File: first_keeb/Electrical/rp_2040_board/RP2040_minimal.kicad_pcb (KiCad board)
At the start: 2 copper layers, 77.4 x 77.1 mm, 72 parts, among them P1 USB-TYPE-C-016, Q1 SN74LV1T34DBV, SW1 SKRKAHE020, SW2 PTS647 SN70 SMTR2 LFS, SW3 PTS647 SN70 SMTR2 LFS, U1 NCP1117-3.3_SOT223, U2 LM4040DBZ-3, U3 PRTR5V0U2X, U4 W25Q32JVSS, U5 RP2040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

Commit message: stm it up
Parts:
- removed H4, H5: MountingHole_4.3mm_M4, MountingHole:MountingHole_4.3mm_M4
- SW2, SW3: footprint Button_Switch_SMD:PTS647_4.5x4.5mm -> Button_Switch_SMD:SW_Push_1P1T_NO_6x6mm_H9.5mm
- moved C13 48.7 mm to (146.7, 85.0)
- moved U2 48.7 mm to (157.4, 85.3)
- moved C14 48.7 mm to (148.5, 85.5)
- moved R1 48.7 mm to (161.1, 86.2)
- moved R4 48.7 mm to (153.9, 86.3)
- moved C15 42.1 mm to (57.8, 49.6), turned to 180 degrees
- moved C12 41.5 mm to (64.3, 67.8)
- moved C10 41.1 mm to (51.7, 64.2)
- moved C11 41.1 mm to (64.8, 66.8)
- moved C16 41.1 mm to (49.5, 60.3)
- moved C17 41.1 mm to (49.5, 63.3)
- moved C3 41.1 mm to (64.6, 62.7)
- moved C4 41.1 mm to (52.3, 65.7)
- moved C5 41.1 mm to (64.6, 63.8)
- moved C6 41.1 mm to (56.5, 59.1)
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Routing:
- net +5V: track 335.9 -> 22.7 mm, vias 14 -> 2
- net +3V3: track 275.9 -> 28.4 mm, vias 2 -> 0
- net Net-(D2-DOUT): track 30.3 -> 1.98 mm
- net Net-(D3-DOUT): track 30.4 -> 2.38 mm
- net Net-(D5-DOUT): track 30.8 -> 2.83 mm
- net Net-(D1-DOUT): track 27.6 -> 2.40 mm
- net Net-(D10-DOUT): track 25.9 -> 3.06 mm
- net /USB_D-: track 23.6 -> 7.99 mm
- net /USB_D+: track 24.1 -> 9.21 mm
- net VBUS: track 20.1 -> 8.45 mm
- net LED_D_3V: track 11.6 -> 0.86 mm
- net RP_ADC1: track 16.1 -> 7.76 mm
- net RP_ADC0: track 21.2 -> 16.2 mm
- net RP_ADC2: track 31.0 -> 26.4 mm
- net GPIO18: track 64.1 -> 62.2 mm
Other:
- board size 77.4 x 77.1 mm -> 65 x 64.7 mm

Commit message: stm32 pcb almost done
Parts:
- moved C10 42.6 mm to (86.5, 88.9)
- moved C16 42.6 mm to (84.3, 85.0)
- moved C17 42.6 mm to (84.3, 87.9)
- moved R7 42.6 mm to (85.8, 74.2)
- moved C11 42.6 mm to (99.5, 91.5)
- moved C12 42.6 mm to (99.1, 92.5)
- moved C15 42.6 mm to (92.6, 74.3)
- moved C3 42.6 mm to (99.4, 87.4)
- moved C5 42.6 mm to (99.4, 88.5)
- moved C6 42.6 mm to (91.3, 83.8)
- moved C7 42.6 mm to (94.6, 83.8)
- moved C8 42.6 mm to (91.5, 93.5)
- moved C9 42.6 mm to (96.3, 93.6)
- moved R5 42.6 mm to (99.4, 89.5)
- moved R6 42.6 mm to (99.4, 90.5)
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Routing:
- net GPIO19: track 83.6 -> 24.1 mm
- net GPIO18: track 62.2 -> 9.68 mm
- net RP_ADC2: track 26.4 -> 0.00 mm
- net Net-(D6-DOUT): track 29.2 -> 3.32 mm
- net RP_ADC0: track 16.2 -> 0.00 mm
- net RP_ADC1: track 7.76 -> 0.00 mm
- net +5V: track 22.7 -> 25.7 mm, vias 2 -> 4
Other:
- board size 65 x 64.7 mm -> 67.1 x 66.8 mm

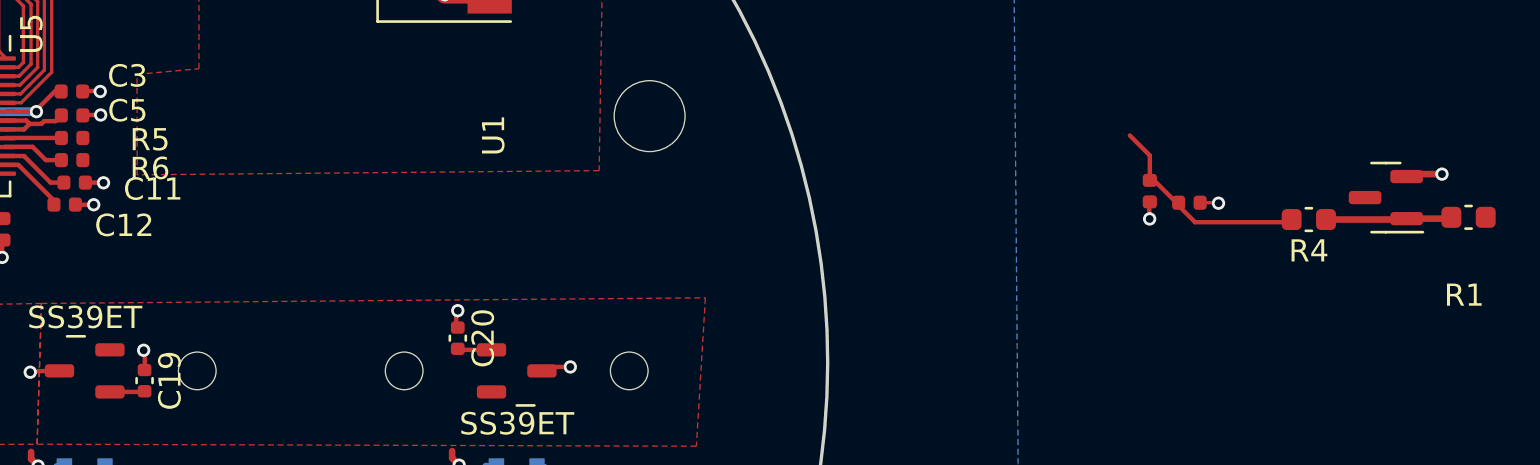
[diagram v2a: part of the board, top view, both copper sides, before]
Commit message: creates plate for pcb
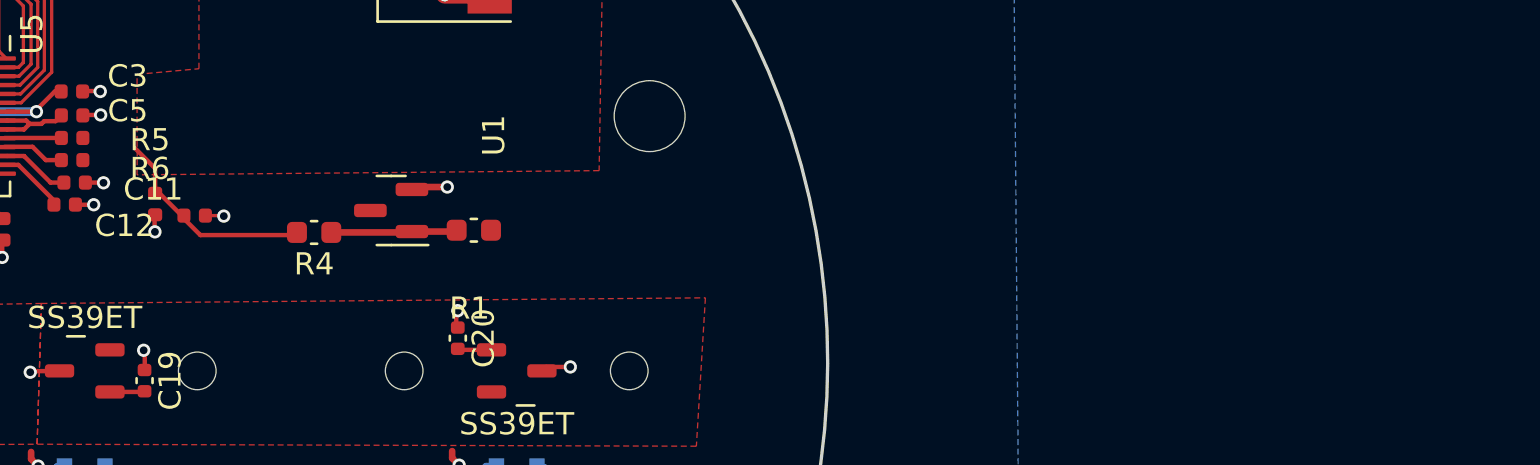
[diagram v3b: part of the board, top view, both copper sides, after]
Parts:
- moved C13 44.9 mm to (103.2, 92.5)
- moved U2 44.9 mm to (113.8, 92.8)
- moved C14 44.9 mm to (105.0, 93.0)
- moved R1 44.9 mm to (117.6, 93.7)
- moved R4 44.9 mm to (110.4, 93.8)
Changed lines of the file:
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@@
   )
   (footprint "Capacitor_SMD:C_0603_1608Metric" (layer "F.Cu")
-    (at 155.2575 93.1675 180)
+    (at 110.355 93.75 180)
     (descr "Capacitor SMD 0603 (1608 Metric), square (rectangular) end terminal, IPC_7351 nominal, (Body size source: IPC-SM-782 page 76, https://www.pcb-3d.com/wordpress/wp-content/uploads/ipc-sm-782a_amendment_1_and_2.pdf), generated with kicad-footprint-generator")
     (tags "capacitor")
@@
   )
   (footprint "Capacitor_SMD:C_0603_1608Metric" (layer "F.Cu")
-    (at 162.4675 93.0675 180)
+    (at 117.565 93.65 180)
     (descr "Capacitor SMD 0603 (1608 Metric), square (rectangular) end terminal, IPC_7351 nominal, (Body size source: IPC-SM-782 page 76, https://www.pcb-3d.com/wordpress/wp-content/uploads/ipc-sm-782a_amendment_1_and_2.pdf), generated with kicad-footprint-generator")
     (tags "capacitor")
@@
   )
   (footprint "Package_TO_SOT_SMD:SOT-23" (layer "F.Cu")
-    (at 158.735 92.1775 180)
+    (at 113.8325 92.76 180)
     (descr "SOT, 3 Pin (https://www.jedec.org/system/files/docs/to-236h.pdf variant AB), generated with kicad-footprint-generator ipc_gullwing_generator.py")
     (tags "SOT TO_SOT_SMD")
@@
   )
   (footprint "Capacitor_SMD:C_0402_1005Metric" (layer "F.Cu")
-    (at 149.865 92.4075)
+    (at 104.9625 92.99)
     (descr "Capacitor SMD 0402 (1005 Metric), square (rectangular) end terminal, IPC_7351 nominal, (Body size source: http://www.tortai-tech.com/upload/download/2011102023233369053.pdf), generated with kicad-footprint-generator")
     (tags "capacitor")
@@
   )
   (footprint "Capacitor_SMD:C_0402_1005Metric" (layer "F.Cu")
-    (at 148.08 91.885 -90)
+    (at 103.1775 92.4675 -90)
     (descr "Capacitor SMD 0402 (1005 Metric), square (rectangular) end terminal, IPC_7351 nominal, (Body size source: http://www.tortai-tech.com/upload/download/2011102023233369053.pdf), generated with kicad-footprint-generator")
     (tags "capacitor")
@@
   (segment (start 96.42 73.915) (end 96.42 73.37) (width 0.25) (layer "F.Cu") (net 1))
   (segment (start 96.42 73.37) (end 96.9 72.89) (width 0.25) (layer "F.Cu") (net 1))
-  (segment (start 151.105 92.4275) (end 151.085 92.4075) (width 0.15) (layer "F.Cu") (net 1))
+  (segment (start 106.2025 93.01) (end 106.1825 92.99) (width 0.15) (layer "F.Cu") (net 1))
   (segment (start 99.5875 92.5) (end 100.405 92.5) (width 0.2) (layer "F.Cu") (net 1))
   (segment (start 78.98 100.07) (end 78.12 100.07) (width 0.2) (layer "F.Cu") (net 1))
@@
   (segment (start 102.71 99.98) (end 102.71 99.16) (width 0.2) (layer "F.Cu") (net 1))
   (segment (start 84.312481 89.209) (end 84.323981 89.2205) (width 0.15) (layer "F.Cu") (net 1))
-  (segment (start 148.055 93.124324) (end 148.071352 93.140676) (width 0.2) (layer "F.Cu") (net 1))
+  (segment (start 103.1525 93.706824) (end 103.168852 93.723176) (width 0.2) (layer "F.Cu") (net 1))
   (segment (start 93.2875 83.81) (end 93.4875 83.61) (width 0.15) (layer "F.Cu") (net 1))
   (segment (start 96.9 72.89) (end 96.635 73.155) (width 0.25) (layer "F.Cu") (net 1))
@@
   (segment (start 103.71625 73.96125) (end 103.77 73.9075) (width 0.25) (layer "F.Cu") (net 1))
   (segment (start 91.295 74.3225) (end 91.81 74.3225) (width 0.15) (layer "F.Cu") (net 1))
-  (segment (start 161.2685 91.1175) (end 160.1125 91.1175) (width 0.3) (layer "F.Cu") (net 1))
+  (segment (start 116.366 91.7) (end 115.21 91.7) (width 0.3) (layer "F.Cu") (net 1))
   (segment (start 78.1 100.07) (end 78.11 100.07) (width 0.2) (layer "F.Cu") (net 1))
-  (segment (start 160.1125 91.1175) (end 159.9485 91.2815) (width 0.3) (layer "F.Cu") (net 1))
+  (segment (start 115.21 91.7) (end 115.046 91.864) (width 0.3) (layer "F.Cu") (net 1))
   (segment (start 116.77 97.352) (end 116.77 97.994) (width 0.2) (layer "F.Cu") (net 1))
   (segment (start 93.4875 83.61) (end 93.8425 83.61) (width 0.15) (layer "F.Cu") (net 1))
@@
   (segment (start 105.784375 80.84) (end 107.115625 80.84) (width 0.6) (layer "F.Cu") (net 1))
   (segment (start 116.25 83.02) (end 117.38 83.02) (width 0.8) (layer "F.Cu") (net 1))
-  (segment (start 148.055 92.490676) (end 148.055 93.124324) (width 0.2) (layer "F.Cu") (net 1))
+  (segment (start 103.1525 93.073176) (end 103.1525 93.706824) (width 0.2) (layer "F.Cu") (net 1))
   (segment (start 85.048481 88.0125) (end 84.632481 88.4285) (width 0.15) (layer "F.Cu") (net 1))
   (segment (start 78.12 100.07) (end 78.05 100.06) (width 0.2) (layer "F.Cu") (net 1))
@@
   (segment (start 88.442981 87.4975) (end 86.482981 85.5375) (width 0.15) (layer "F.Cu") (net 1))
   (segment (start 103.365 73.135) (end 104.13 73.135) (width 0.25) (layer "F.Cu") (net 1))
-  (segment (start 151.085 92.4075) (end 150.362831 92.4075) (width 0.15) (layer "F.Cu") (net 1))
+  (segment (start 106.1825 92.99) (end 105.460331 92.99) (width 0.15) (layer "F.Cu") (net 1))
   (via (at 85.285 88.0125) (size 0.6) (drill 0.35) (layers "F.Cu" "B.Cu") (net 1))
   (via (at 80.412481 86.3485) (size 0.6) (drill 0.35) (layers "F.Cu" "B.Cu") (net 1))
@@
   (via (at 81.812481 91.0485) (size 0.6) (drill 0.35) (layers "F.Cu" "B.Cu") (net 1))
   (via (at 93.2875 83.81) (size 0.6) (drill 0.35) (layers "F.Cu" "B.Cu") (free) (net 1))
-  (via (at 161.2685 91.1175) (size 0.6) (drill 0.35) (layers "F.Cu" "B.Cu") (net 1))
+  (via (at 116.366 91.7) (size 0.6) (drill 0.35) (layers "F.Cu" "B.Cu") (net 1))
   (via (at 90.1775 93.535) (size 0.6) (drill 0.35) (layers "F.Cu" "B.Cu") (net 1))
   (via (at 86.482981 85.5375) (size 0.6) (drill 0.35) (layers "F.Cu" "B.Cu") (net 1))
-  (via (at 148.071352 93.140676) (size 0.6) (drill 0.35) (layers "F.Cu" "B.Cu") (net 1))
+  (via (at 103.168852 93.723176) (size 0.6) (drill 0.35) (layers "F.Cu" "B.Cu") (net 1))
   (via (at 103.71625 73.96125) (size 0.6) (drill 0.35) (layers "F.Cu" "B.Cu") (free) (net 1))
   (via (at 89.8975 83.76) (size 0.6) (drill 0.35) (layers "F.Cu" "B.Cu") (net 1))
@@
   (via (at 100.7 87.3875) (size 0.6) (drill 0.35) (layers "F.Cu" "B.Cu") (net 1))
   (via (at 85.562996 90.3625) (size 0.6) (drill 0.35) (layers "F.Cu" "B.Cu") (net 1))
-  (via (at 151.18 92.43) (size 0.6) (drill 0.35) (layers "F.Cu" "B.Cu") (net 1))
+  (via (at 106.2775 93.0125) (size 0.6) (drill 0.35) (layers "F.Cu" "B.Cu") (net 1))
   (via (at 83.218162 85.27) (size 0.6) (drill 0.35) (layers "F.Cu" "B.Cu") (net 1))
   (segment (start 81.383 112.618) (end 81.663 112.618) (width 0.15) (layer "B.Cu") (net 1))
@@
   (segment (start 116.903 104.473) (end 117.41 104.98) (width 0.3) (layer "B.Cu") (net 36))
   (segment (start 97.896999 104.836999) (end 97.96 104.9) (width 0.3) (layer "B.Cu") (net 36))
-  (segment (start 161.4725 93.1275) (end 159.6725 93.1275) (width 0.3) (layer "F.Cu") (net 37))
-  (segment (start 159.6725 93.1275) (end 159.6325 93.1675) (width 0.3) (layer "F.Cu") (net 37))
-  (segment (start 159.6325 93.1675) (end 156.0325 93.1675) (width 0.3) (layer "F.Cu") (net 37))
-  (segment (start 161.5525 93.1675) (end 161.5315 93.1465) (width 0.3) (layer "F.Cu") (net 37))
+  (segment (start 116.57 93.71) (end 114.77 93.71) (width 0.3) (layer "F.Cu") (net 37))
+  (segment (start 114.77 93.71) (end 114.73 93.75) (width 0.3) (layer "F.Cu") (net 37))
+  (segment (start 114.73 93.75) (end 111.13 93.75) (width 0.3) (layer "F.Cu") (net 37))
+  (segment (start 116.65 93.75) (end 116.629 93.729) (width 0.3) (layer "F.Cu") (net 37))
   (segment (start 96.383376 89.485) (end 98.945876 89.485) (width 0.2) (layer "F.Cu") (net 41))
   (segment (start 97.645876 89.885) (end 98.245876 90.485) (width 0.2) (layer "F.Cu") (net 42))
@@
   (segment (start 101.8 74.685) (end 101.8 74.105) (width 0.15) (layer "F.Cu") (net 51))
   (segment (start 103.6 75.935) (end 103.05 75.935) (width 0.15) (layer "F.Cu") (net 51))
-  (segment (start 154.69 93.2875) (end 150.1225 93.2875) (width 0.2) (layer "F.Cu") (net 52))
-  (segment (start 150.1225 93.2875) (end 149.285 92.45) (width 0.2) (layer "F.Cu") (net 52))
-  (segment (start 148.08 90.275) (end 147.1775 89.3725) (width 0.2) (layer "F.Cu") (net 52))
-  (segment (start 148.08 91.4) (end 148.275 91.4) (width 0.2) (layer "F.Cu") (net 52))
-  (segment (start 148.08 91.4) (end 148.08 90.275) (width 0.2) (layer "F.Cu") (net 52))
-  (segment (start 148.275 91.4) (end 149.305 92.43) (width 0.2) (layer "F.Cu") (net 52))
+  (segment (start 109.7875 93.87) (end 105.22 93.87) (width 0.2) (layer "F.Cu") (net 52))
+  (segment (start 105.22 93.87) (end 104.3825 93.0325) (width 0.2) (layer "F.Cu") (net 52))
+  (segment (start 103.1775 90.8575) (end 102.275 89.955) (width 0.2) (layer "F.Cu") (net 52))
+  (segment (start 103.1775 91.9825) (end 103.3725 91.9825) (width 0.2) (layer "F.Cu") (net 52))
+  (segment (start 103.1775 91.9825) (end 103.1775 90.8575) (width 0.2) (layer "F.Cu") (net 52))
+  (segment (start 103.3725 91.9825) (end 104.4025 93.0125) (width 0.2) (layer "F.Cu") (net 52))
   (segment (start 98.34 74.765) (end 98.272 74.833) (width 0.15) (layer "F.Cu") (net 53))
   (segment (start 98.25 74.895) (end 98.242 74.903) (width 0.15) (layer "F.Cu") (net 53))

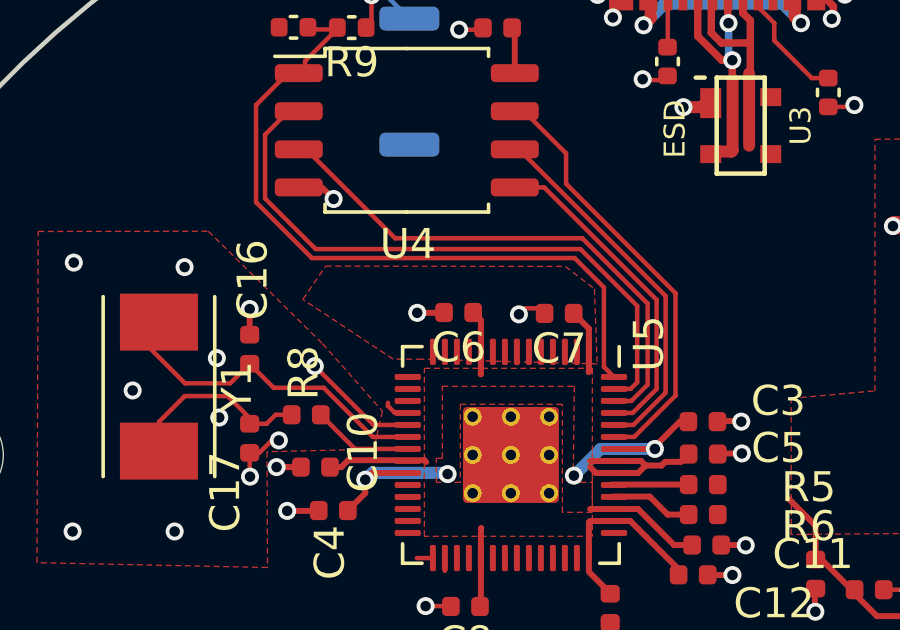
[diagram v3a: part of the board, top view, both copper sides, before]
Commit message: v1 stm ordered
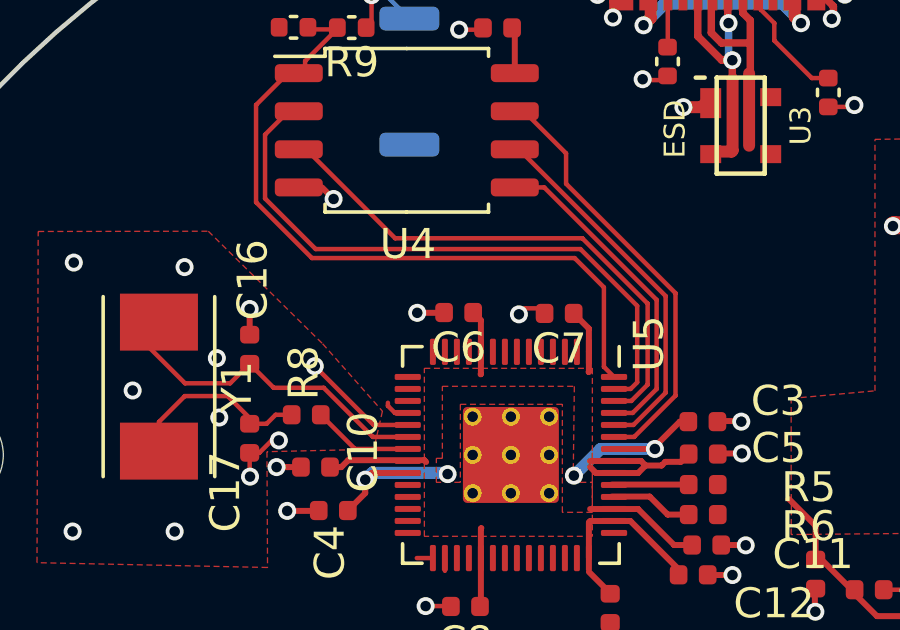
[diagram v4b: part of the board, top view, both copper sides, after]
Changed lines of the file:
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@@
-  )
-  (zone (net 5) (net_name "+3V3") (layer "F.Cu") (hatch edge 0.5)
-    (priority 3)
-    (connect_pads (clearance 0.25))
-    (min_thickness 0.25) (filled_areas_thickness no)
-    (fill yes (thermal_gap 0.5) (thermal_bridge_width 0.5))
-    (polygon
-      (pts
-        (xy 89.095 85.3025)
-        (xy 86.085 83.3125)
-        (xy 86.845 82.2025)
-        (xy 94.835 82.2125)
-        (xy 95.805 82.9625)
-        (xy 95.895 85.4625)
-        (xy 90.05 85.305)
-      )
-    )
   )
   (zone (net 5) (net_name "+3V3") (layer "F.Cu") (hatch edge 0.5)
@@
       43cd5bd8-00d0-4719-822a-279fb55d146a
       44500a0c-3f51-45bf-8408-0bf1db6cffc7
-      45ccfcff-6274-4bfa-b347-b3be63b787d5
       45fba069-e9ef-4b34-a26c-d09566859d52
       47708e40-8969-4df5-95d2-e371cc7f88d0
